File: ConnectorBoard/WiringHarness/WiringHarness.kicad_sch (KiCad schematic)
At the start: 21 parts, among them J1 Barrel_Jack, J2 Conn_01x03, J3 Conn_01x03, J4 Conn_02x05_Odd_Even, J5 Socket, J6 Qwiic, J7 Header, U1 L7805, U2 TLV75533PDBV

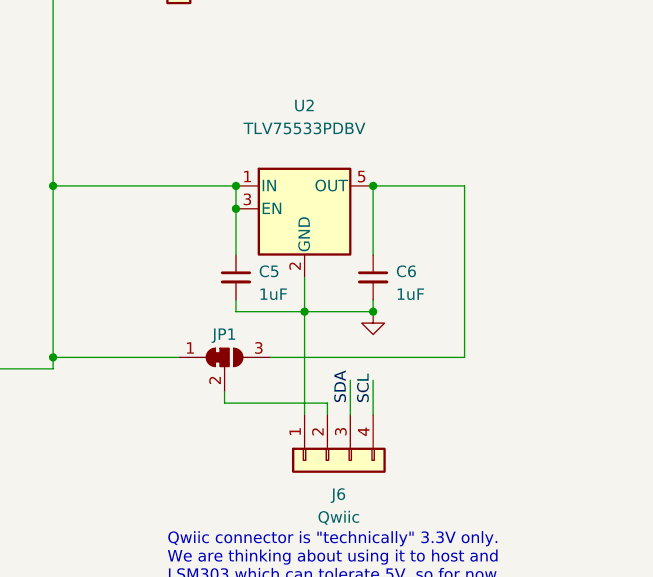
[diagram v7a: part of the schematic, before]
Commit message: add pullups for 3.3 version of I2C bus.
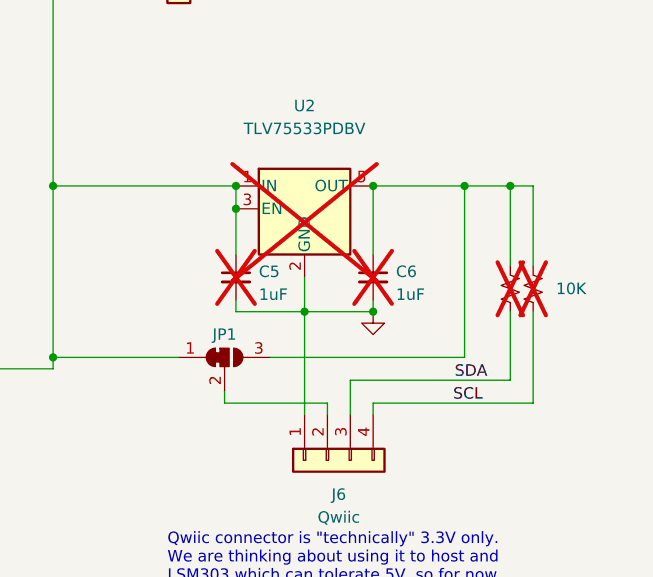
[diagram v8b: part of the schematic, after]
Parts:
- added R1, R2: 10K, Resistor_SMD:R_0603_1608Metric, symbol Device:R_Small_US
- C1, C2: Vendor (none) -> 445-5950-1-ND
- C3, C4: Digikey (none) -> 1276-1861-1-ND; Vendor (none) -> 1276-1861-1-ND
- C5, C6: Digikey (none) -> 1276-1861-1-ND; Vendor (none) -> 1276-1861-1-ND; now not fitted
- D1: Digikey (none) -> SK36A-LTPMSCT-ND; Vendor (none) -> SK36A-LTPMSCT-ND
- J1: Digikey (none) -> CP-002A-ND; Vendor (none) -> CP-002A-ND
- J2, J3: Digikey (none) -> PH1RB-03-UA; Vendor (none) -> PH1RB-03-UA
- J4: Vendor (none) -> 732-2094-ND
- J5: Digikey (none) -> S7039-ND; Vendor (none) -> S7039-ND
- J6: Digikey (none) -> SM04B-SRSS-TB; Vendor (none) -> SM04B-SRSS-TB
- J7: Digikey (none) -> S4B-PH-K-S; Vendor (none) -> S4B-PH-K-S
- U1: Vendor (none) -> NCV7805BDTRKG
- U2: Digikey (none) -> 296-50411-1-ND; Vendor (none) -> 296-50411-1-ND; now not fitted
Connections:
- net SCL: now also R1.2
- net SDA: now also R2.2
- net at C6.1, JP1.3 (B), U2.5 (OUT): now also R1.1, R2.1
